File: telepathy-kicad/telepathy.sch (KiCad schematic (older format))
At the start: 71 parts, among them K1 CONN_3, P1 CONN_2, P2 CONN_4, P3 CONN_4, P4 CONN_4, P5 CONN_4, Q1 NPN, Q2 NPN, Q3 NPN, Q4 NPN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

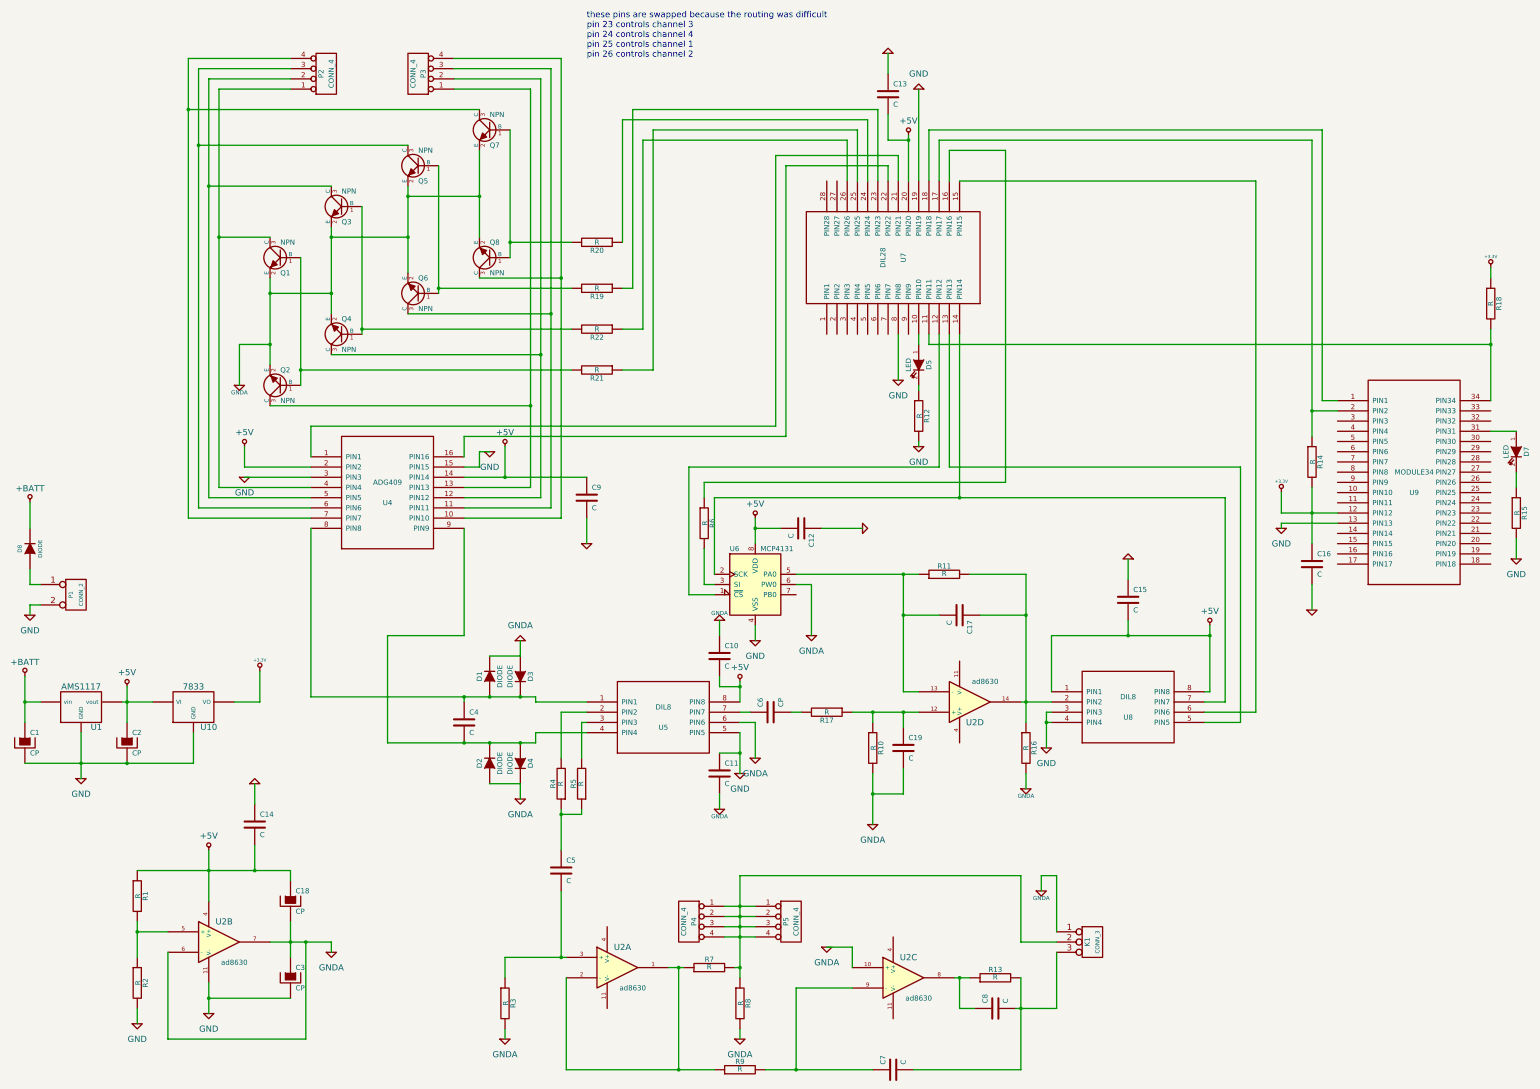
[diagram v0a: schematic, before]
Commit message: added bootloader and makefiles
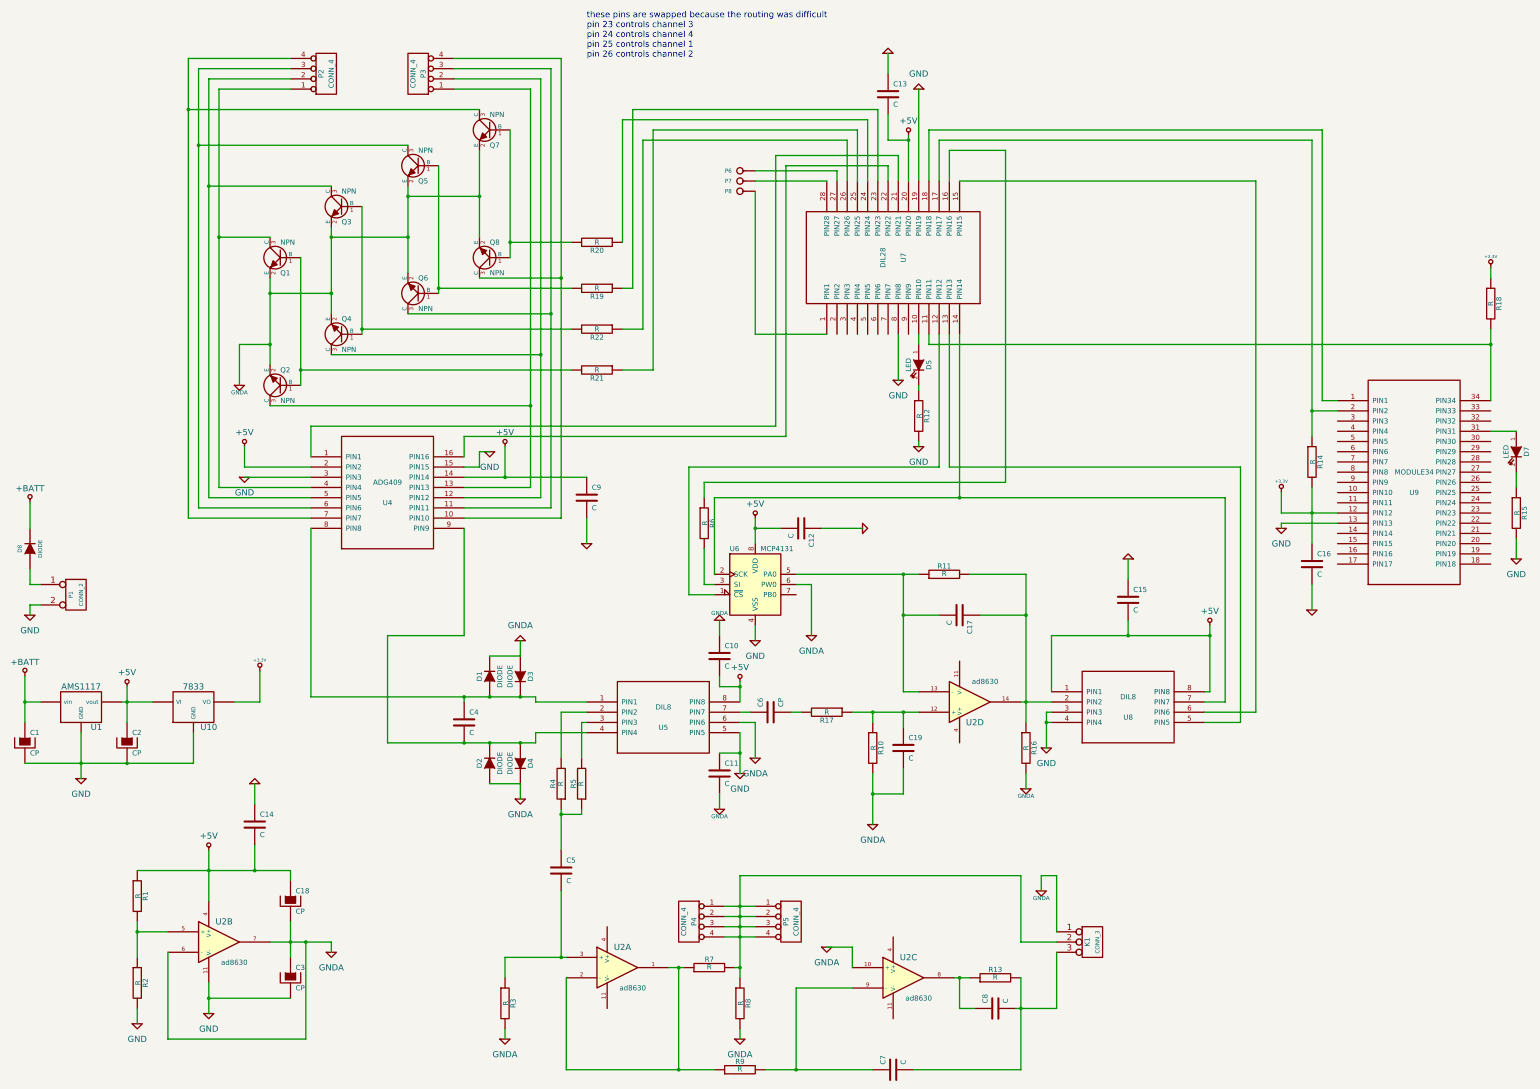
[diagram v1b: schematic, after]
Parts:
- added P6, P7, P8: CONN_1, symbol CONN_1
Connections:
- net at U7.1 (PIN1): now also P8.1
- net at U7.27 (PIN27): now also P6.1
- net at U7.28 (PIN28): now also P7.1

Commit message: added noncontact electrodes
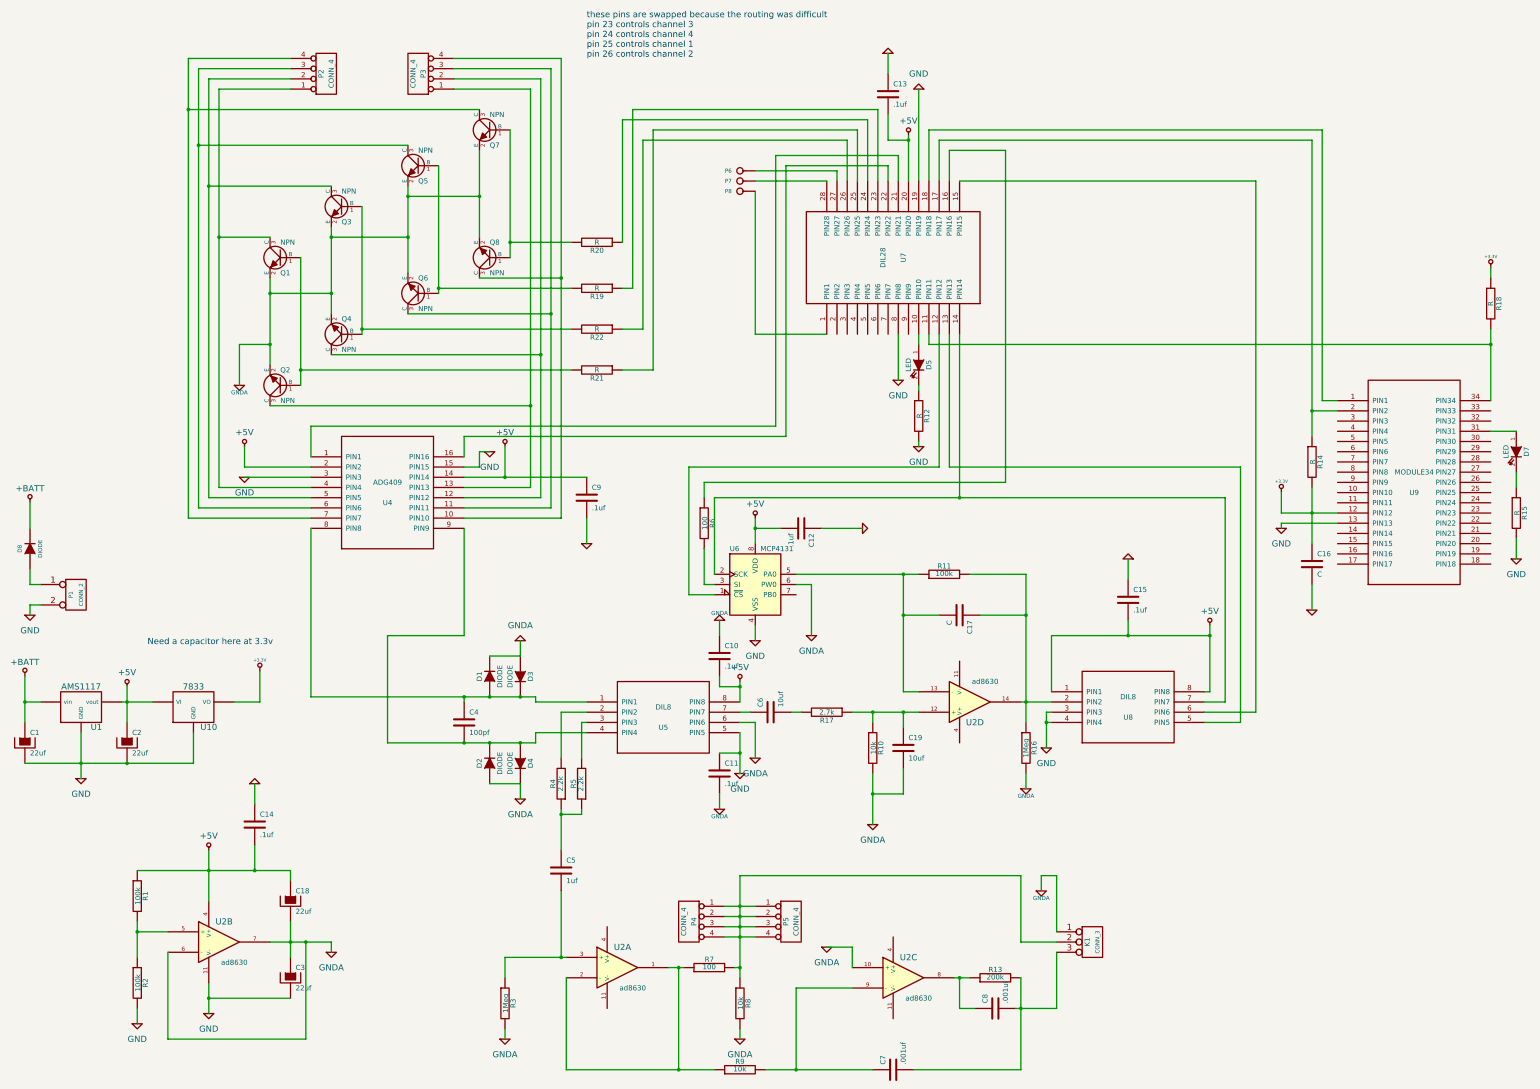
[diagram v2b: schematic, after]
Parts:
- C1, C18, C2, C3: value CP -> 22uf
- C10, C11, C12, C13, C14, C15, C9: value C -> .1uf
- C19: value C -> 10uf
- C4: value C -> 100pf
- C5: value C -> 1uf
- C6: value CP -> 10uf
- C7, C8: value C -> .001uf
- R1, R11, R2: value R -> 100k
- R10, R8, R9: value R -> 10k
- R13: value R -> 200k
- R16, R3: value R -> 1Meg
- R17: value R -> 2.7k
- R4, R5: value R -> 2.2k
- R6, R7: value R -> 100
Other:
- note added: "Need a capacitor here at 3.3v\n"
